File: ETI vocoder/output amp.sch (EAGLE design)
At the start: 18 parts, among them IC1 LM1458N, IC2 LM741P, J1 22-23-2031, X2 22-23-2051, X3 22-23-2021

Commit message: Fixed input boards in regards to article and added spacer holes
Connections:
- net RETURN renamed FX_RETURN
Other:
- note added: "FX return here is output."
- note added: "Har sjekket footprint caps"
- note added: "Har sjekket retning på pots"
- note added: "Use jumper between mix and return if no fx module used"
- note added: "or use mix as output"
- note removed: "Sjekk retning på pots"
- note removed: "Use jumper if no fx module used"
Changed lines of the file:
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@@
 <?xml version="1.0" encoding="utf-8"?>
 <!DOCTYPE eagle SYSTEM "eagle.dtd">
-<eagle version="7.2.0">
+<eagle version="6.2">
 <drawing>
 <settings>
@@
 <sheet>
 <plain>
-<text x="203.2" y="10.16" size="1.778" layer="97">Use jumper if no fx module used</text>
-<text x="154.94" y="139.7" size="1.778" layer="91">Sjekk retning på pots</text>
+<text x="205.74" y="30.48" size="1.778" layer="97">Use jumper between mix and return if no fx module used</text>
+<text x="154.94" y="139.7" size="1.778" layer="91">Har sjekket retning på pots</text>
+<text x="205.74" y="7.62" size="1.778" layer="97">FX return here is output.</text>
+<text x="205.74" y="27.94" size="1.778" layer="97">or use mix as output</text>
+<text x="154.94" y="134.62" size="1.778" layer="91">Har sjekket footprint caps</text>
 </plain>
 <instances>
@@
 </segment>
 </net>
-<net name="RETURN" class="0">
+<net name="FX_RETURN" class="0">
 <segment>
 <wire x1="226.06" y1="25.4" x2="205.74" y2="25.4" width="0.1524" layer="91"/>

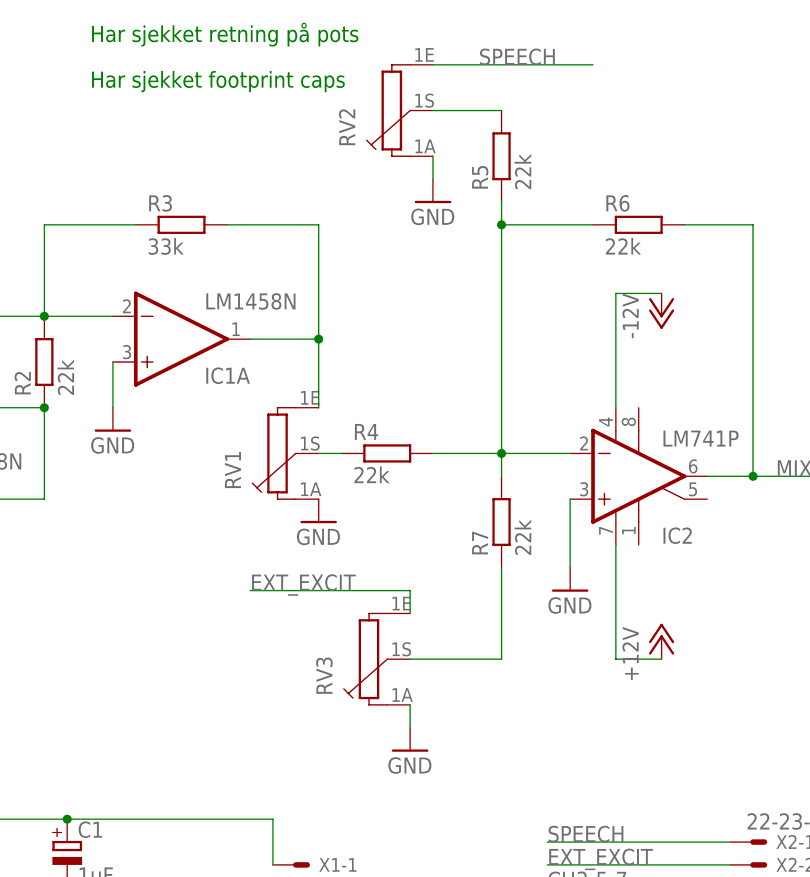
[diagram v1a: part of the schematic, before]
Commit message: Finished first of two halves of the universal voice board
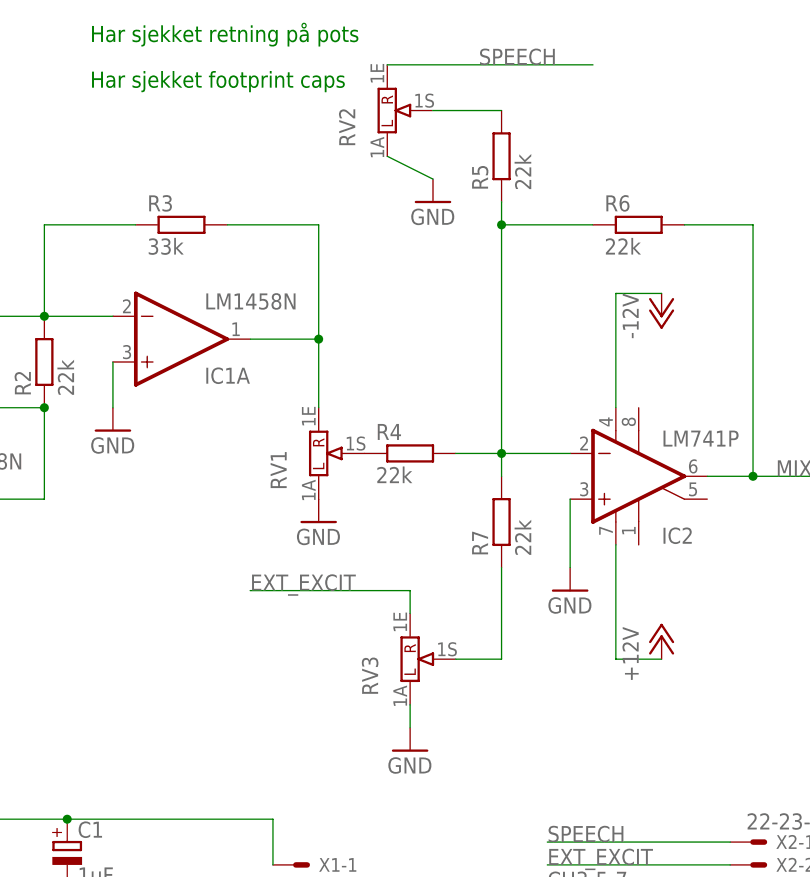
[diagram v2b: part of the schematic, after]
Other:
- moved on the sheet: R4
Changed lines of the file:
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@@
 </plain>
 <instances>
-<instance part="RV1" gate="G$1" x="175.26" y="93.98" smashed="yes" rot="R90">
-<attribute name="NAME" x="171.704" y="89.916" size="1.778" layer="95" rot="R90"/>
+<instance part="RV1" gate="G$1" x="180.34" y="93.98" smashed="yes" rot="R90">
+<attribute name="NAME" x="176.784" y="89.916" size="1.778" layer="95" rot="R90"/>
 </instance>
-<instance part="RV3" gate="G$1" x="185.42" y="71.12" smashed="yes" rot="R90">
-<attribute name="NAME" x="181.864" y="67.056" size="1.778" layer="95" rot="R90"/>
+<instance part="RV3" gate="G$1" x="190.5" y="71.12" smashed="yes" rot="R90">
+<attribute name="NAME" x="186.944" y="67.056" size="1.778" layer="95" rot="R90"/>
 </instance>
 <instance part="RV2" gate="G$1" x="187.96" y="132.08" smashed="yes" rot="R90">
@@
 <instance part="R2" gate="G$1" x="149.86" y="104.14" rot="R90"/>
 <instance part="R3" gate="G$1" x="165.1" y="119.38"/>
-<instance part="R4" gate="G$1" x="187.96" y="93.98"/>
+<instance part="R4" gate="G$1" x="190.5" y="93.98"/>
 <instance part="R5" gate="G$1" x="200.66" y="127" rot="R90"/>
 <instance part="R6" gate="G$1" x="215.9" y="119.38"/>
@@
 <pinref part="RV1" gate="G$1" pin="1S"/>
 <pinref part="R4" gate="G$1" pin="1"/>
-<wire x1="182.88" y1="93.98" x2="180.34" y2="93.98" width="0.1524" layer="91"/>
 </segment>
 </net>
@@
 <pinref part="RV2" gate="G$1" pin="1A"/>
 <pinref part="GND5" gate="1" pin="GND"/>
-<wire x1="193.04" y1="127" x2="193.04" y2="124.46" width="0.1524" layer="91"/>
+<wire x1="187.96" y1="127" x2="193.04" y2="124.46" width="0.1524" layer="91"/>
 </segment>
 <segment>
@@
 <wire x1="200.66" y1="81.28" x2="200.66" y2="71.12" width="0.1524" layer="91"/>
 <pinref part="RV3" gate="G$1" pin="1S"/>
-<wire x1="200.66" y1="71.12" x2="190.5" y2="71.12" width="0.1524" layer="91"/>
+<wire x1="200.66" y1="71.12" x2="195.58" y2="71.12" width="0.1524" layer="91"/>
 </segment>
 </net>
@@
 <segment>
 <pinref part="R4" gate="G$1" pin="2"/>
-<wire x1="193.04" y1="93.98" x2="200.66" y2="93.98" width="0.1524" layer="91"/>
+<wire x1="195.58" y1="93.98" x2="200.66" y2="93.98" width="0.1524" layer="91"/>
 <pinref part="R7" gate="G$1" pin="2"/>
 <wire x1="200.66" y1="93.98" x2="200.66" y2="91.44" width="0.1524" layer="91"/>
@@
 <segment>
 <pinref part="RV2" gate="G$1" pin="1E"/>
-<wire x1="193.04" y1="137.16" x2="210.82" y2="137.16" width="0.1524" layer="91"/>
+<wire x1="187.96" y1="137.16" x2="210.82" y2="137.16" width="0.1524" layer="91"/>
 <label x="198.12" y="137.16" size="1.778" layer="95"/>
 </segment>
